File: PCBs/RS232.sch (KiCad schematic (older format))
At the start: 9 parts, among them J3 USB_B, U3 FT232RL

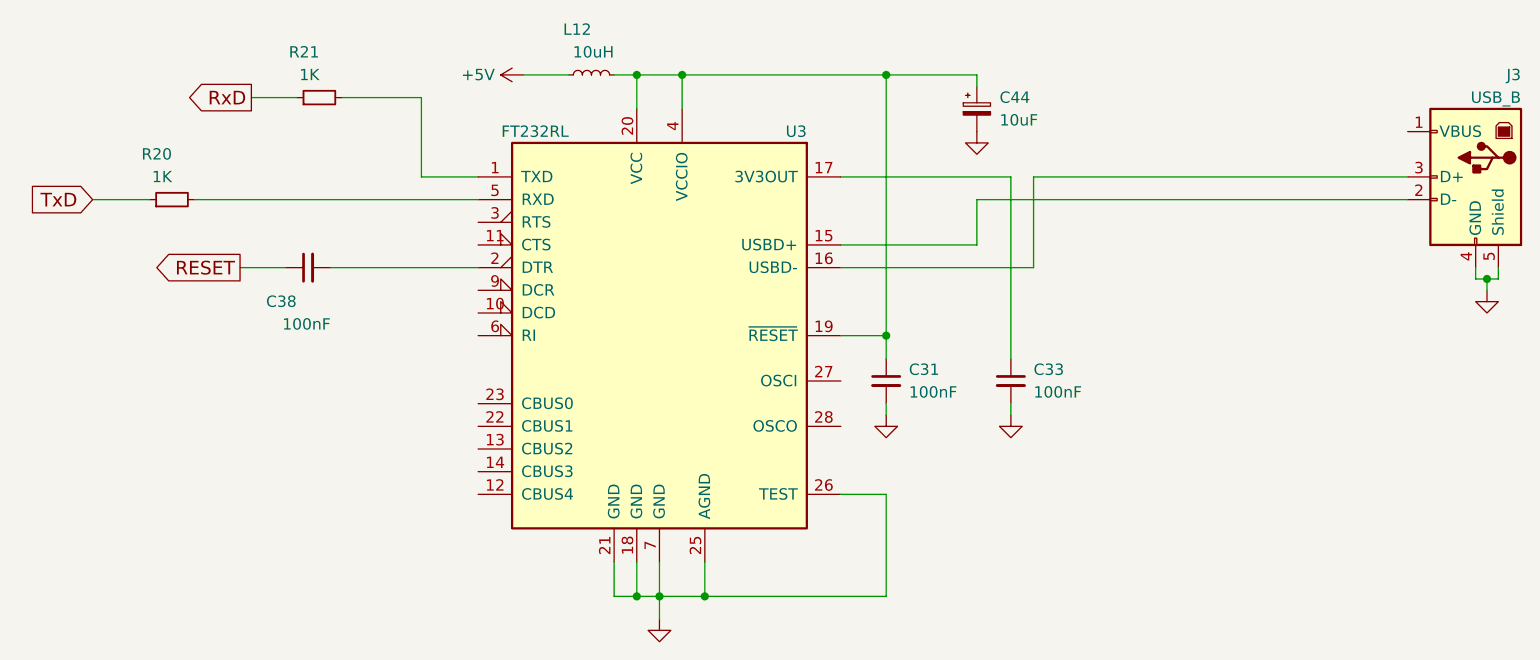
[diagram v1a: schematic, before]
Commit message: discret, simple, CH340E
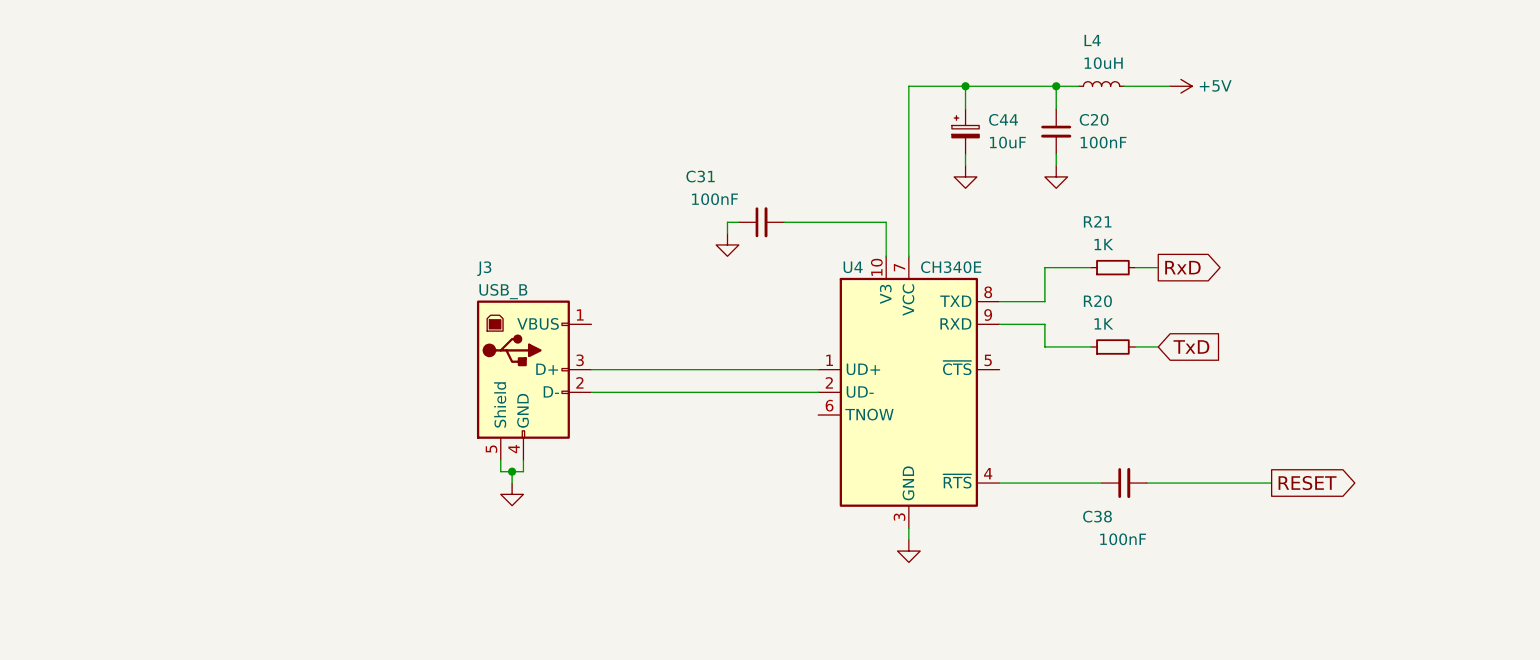
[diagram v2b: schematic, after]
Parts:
- removed C33: 100nF, LCSDR:C_1206_0603, symbol C_Small
- removed L12: 10uH, Choke_Axial_ThroughHole:Choke_Horizontal_RM10mm, symbol L_Small
- removed U3: FT232RL, Housings_SSOP:SSOP-28_5.3x10.2mm_Pitch0.65mm, symbol FT232RL
- added C20: 100nF, Capacitors_SMD:C_0603_HandSoldering, symbol C_Small
- added L4: 10uH, Choke_Axial_ThroughHole:Choke_Horizontal_RM10mm, symbol L_Small
- added U4: CH340E, Housings_SSOP:MSOP-10_3x3mm_Pitch0.5mm, symbol CH340E
- C31, C38: footprint LCSDR:C_1206_0603 -> Capacitors_SMD:C_0603_HandSoldering
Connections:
- net +5V: now also L4.2
- net GND: now also C31.1, C20.2, U4.3 (GND); no longer C31.2
- net RESET: now also C38.2; no longer C38.1
- net RxD: now also R21.2; no longer R21.1
- net TxD: now also R20.2; no longer R20.1
- net at C44.1: now also C20.1, L4.1, U4.7 (VCC); no longer C31.1
- net at J3.2 (D-): now also U4.2 (UD-)
- net at J3.3 (D+): now also U4.1 (UD+)
- new net: C38.1, U4.4 (~RTS)
- new net: R20.1, U4.9 (RXD)
- new net: R21.1, U4.8 (TXD)
- new net: C31.2, U4.10 (V3)
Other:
- moved on the sheet: C38, C44, R20, R21
